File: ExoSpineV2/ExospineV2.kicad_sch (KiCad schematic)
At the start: 30 parts, among them J1 GPIO, J20 S2B-PH-K-S(LF)(SN), J21 S2B-PH-K-S(LF)(SN), J22 S2B-PH-K-S(LF)(SN), J23 S2B-PH-K-S(LF)(SN), J24 Conn_01x02, J25 Conn_01x03, J26 Conn_01x03, J27 Conn_01x04, J28 Conn_01x03, J29 Conn_01x03, Q6 Q_NMOS_DGS, Q7 Q_NMOS_DGS, U6 MCP3008

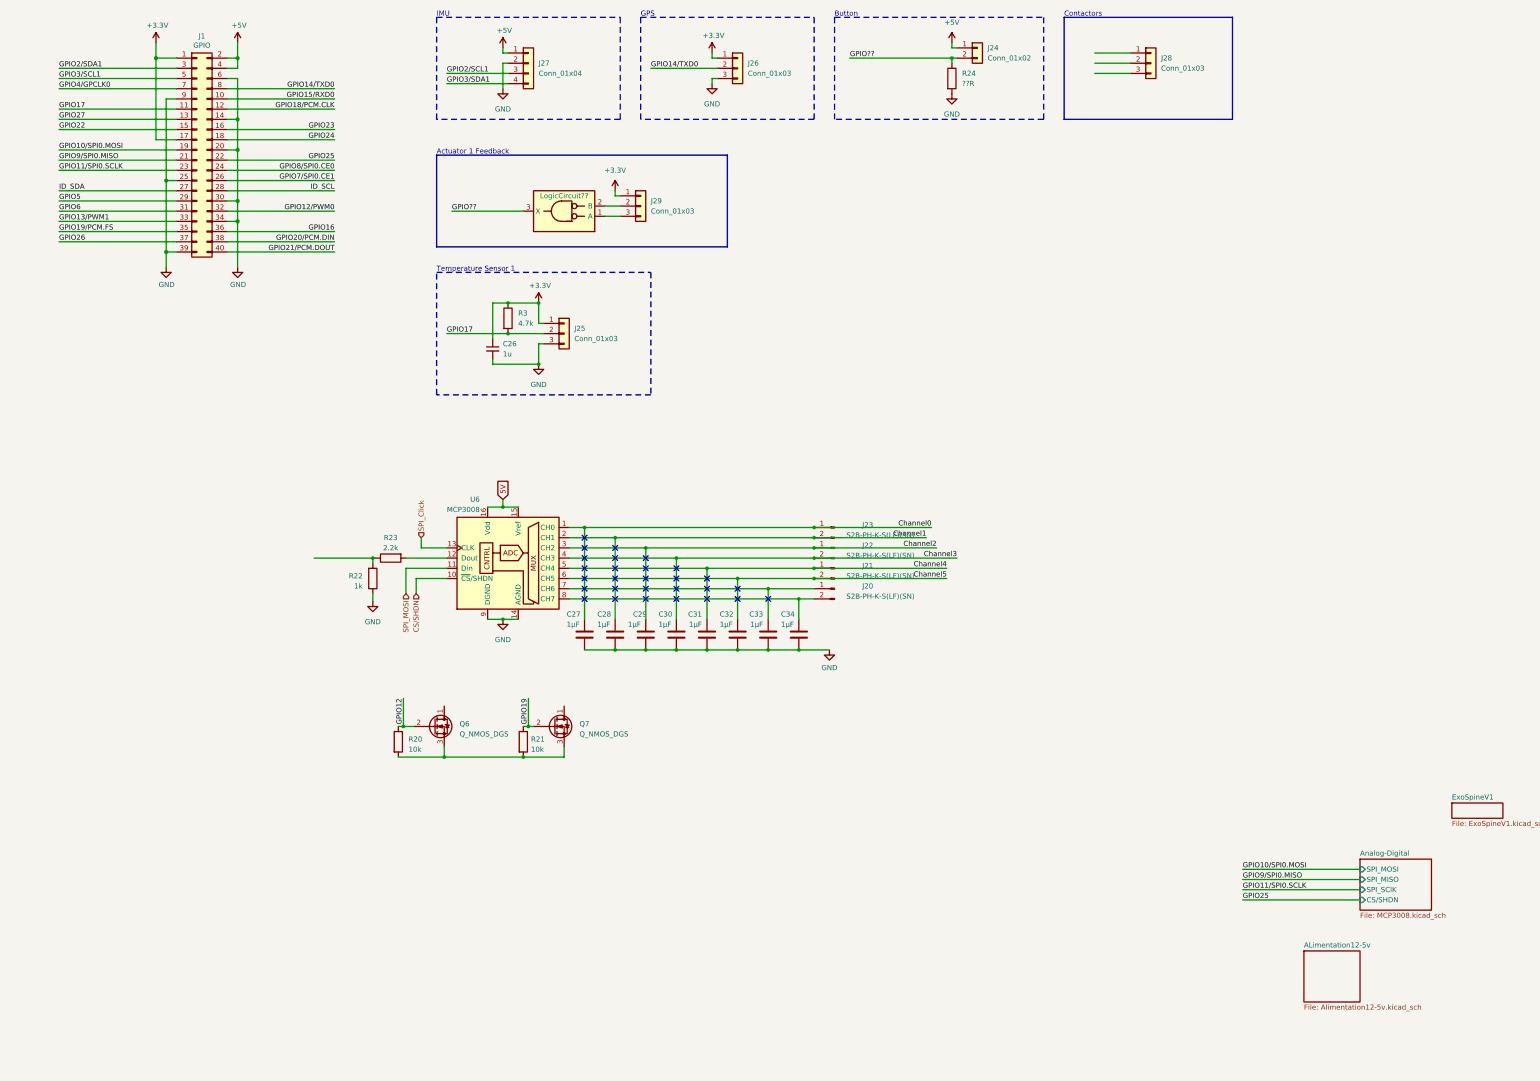
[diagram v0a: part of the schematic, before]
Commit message: MCP3008 circuit
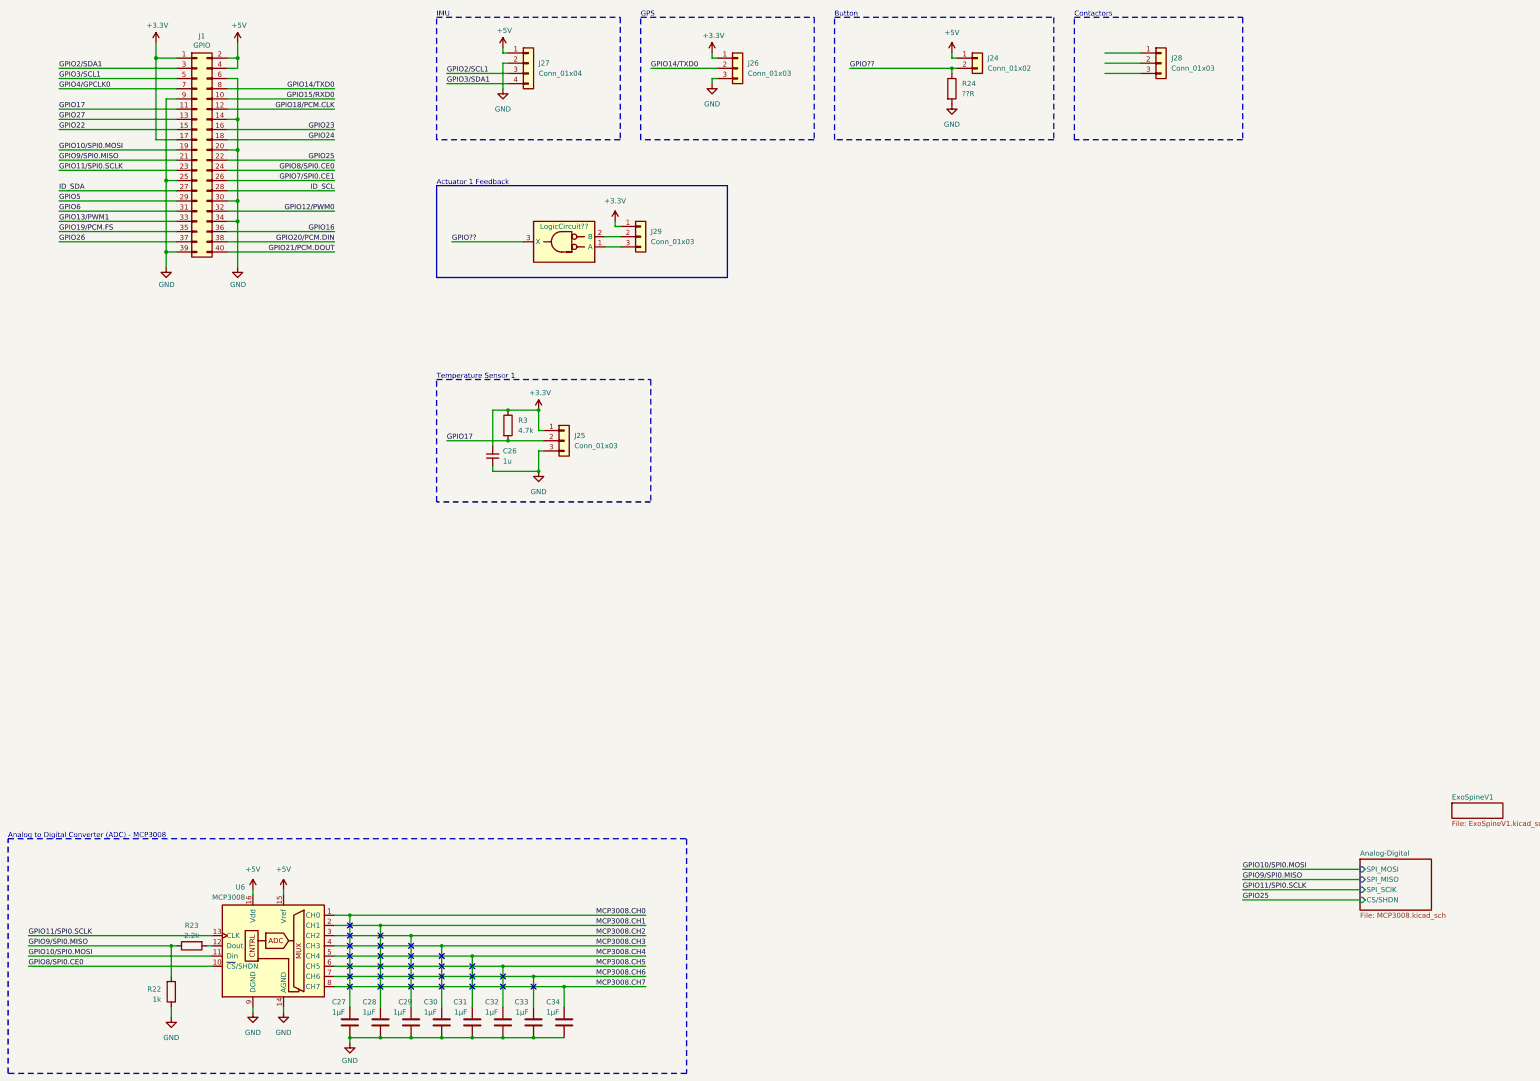
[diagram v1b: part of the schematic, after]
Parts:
- removed J20, J21, J22, J23: S2B-PH-K-S(LF)(SN), Connector_PinHeader_2.00mm:PinHeader_1x02_P2.00mm_Vertical, symbol Connector:Conn_01x02_Pin
- removed Q6, Q7: Q_NMOS_DGS, symbol Device:Q_NMOS_DGS
- removed R20, R21: 10k, symbol Device:R
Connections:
- net 5V is gone; now on net +5V: U6.15 (Vref), U6.16 (Vdd)
- net CS/SHDN is gone; now on net GPIO8/SPI0.CE0: U6.10 (~{CS}/SHDN)
- net SPI_Click is gone; now on net GPIO11/SPI0.SCLK: U6.13 (CLK)
- net SPI_MOSI is gone; now on net GPIO10/SPI0.MOSI: U6.11 (Din)
- net GPIO9/SPI0.MISO: now also R22.2, R23.1
- net MCP3008.CH6: now reaches C33.1, U6.7 (CH6)
- net MCP3008.CH7: now reaches C34.1, U6.8 (CH7)
- net Channel0 renamed MCP3008.CH0
- net Channel1 renamed MCP3008.CH1
- net Channel2 renamed MCP3008.CH2
- net Channel3 renamed MCP3008.CH3
- net Channel4 renamed MCP3008.CH4
- net Channel5 renamed MCP3008.CH5
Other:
- removed sheet ALimentation12-5v
- note added: "Analog to Digital Converter (ADC) - MCP3008"
- moved on the sheet: C26, C27, C28, C29, C30, C31, C32, C33, C34, J24, J25, J28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

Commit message: Actuator Control 1
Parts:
- added J15: Conn_01x02, symbol Connector_Generic:Conn_01x02
- added Q6: Q_NMOS_DGS, symbol Device:Q_NMOS_DGS
- added R10: 10k, symbol Device:R
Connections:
- net GND: now also Q6.3 (S), R10.2
- new net: J15.2 (Pin_2), Q6.1 (D)
- new net +12V: J15.1 (Pin_1)
- new net GPIO12: Q6.2 (G), R10.1
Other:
- removed sheet Analog-Digital
- note added: "Actuator Control 1"
- note added: "Actuator Feedback 1"
- note removed: "Actuator 1 Feedback"
- moved on the sheet: C26, J25, J29, LogicCircuit??, R3

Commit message: Actuator Control 2 and backup
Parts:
- added J16, J17: Conn_01x02, symbol Connector_Generic:Conn_01x02
- added Q7, Q8: Q_NMOS_DGS, symbol Device:Q_NMOS_DGS
- added R11, R12: 10k, symbol Device:R
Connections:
- net GPIO2/SCL1 is gone; now on net GPIO2/SDA1: J27.3 (Pin_3)
- net GPIO3/SDA1 is gone; now on net GPIO3/SCL1: J27.4 (Pin_4)
- net +12V: now also J16.1 (Pin_1), J17.1 (Pin_1)
- net GND: now also Q7.3 (S), Q8.3 (S), R11.2, R12.2
- net GPIO17: no longer J25.2 (Pin_2), R3.2
- net GPIO22: now also Q8.2 (G), R12.1
- net GPIO25: now also J24.2 (Pin_2), R24.1
- net GPIO27: now also Q7.2 (G), R11.1
- net GPIO5: now also J25.2 (Pin_2), R3.2
- net GPIO??: no longer J24.2 (Pin_2), R24.1
- new net: J16.2 (Pin_2), Q7.1 (D)
- new net: J17.2 (Pin_2), Q8.1 (D)
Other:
- note added: "Actuator Control 2"
- note added: "Actuator Control Backup"
- moved on the sheet: C26, J15, J25, J27, Q6, R10, R3

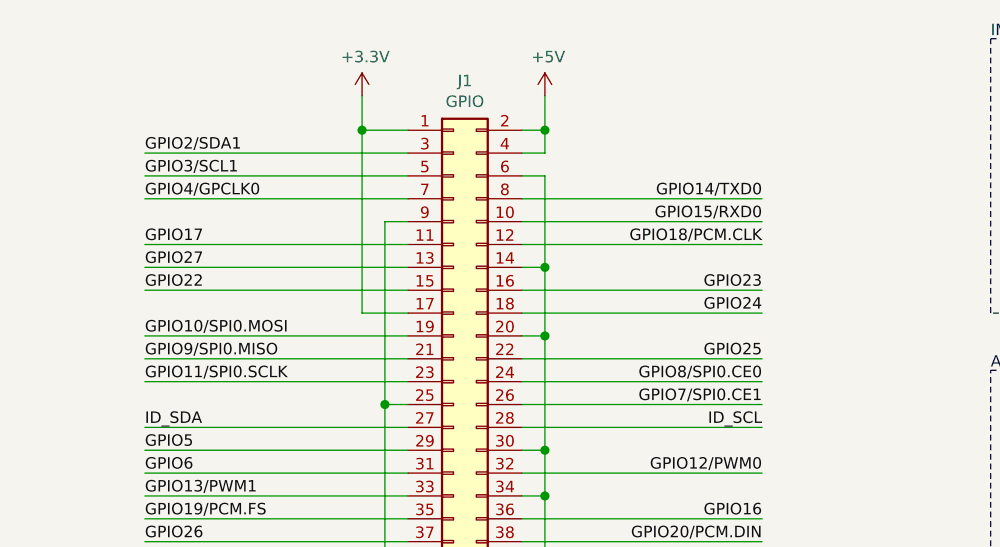
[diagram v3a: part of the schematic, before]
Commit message: Identified RP pins
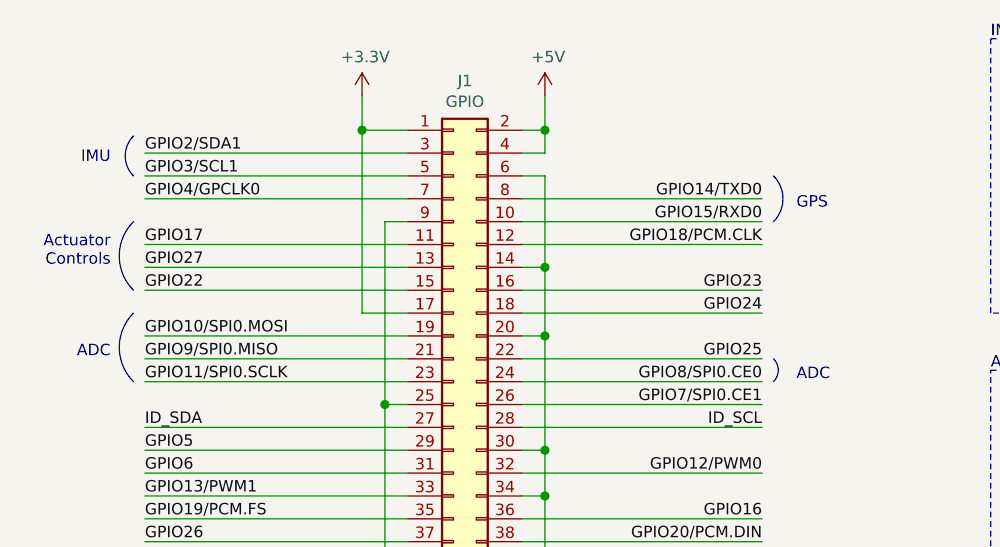
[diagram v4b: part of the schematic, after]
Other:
- note added: "ADC"
- note added: "Actuator Controls"
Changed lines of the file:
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@@
+    (fill (type none))
+  )
+  (arc (start 101.6 33.02) (mid 102.6521 35.56) (end 101.6 38.1)
+    (stroke (width 0) (type default) (color 132 132 132 1))
     (fill (type none))
   )
@@
   (rectangle (start 176.53 17.78) (end 219.71 48.26)
     (stroke (width 0) (type dash))
+    (fill (type none))
+  )
+  (arc (start 30.48 45.72) (mid 28.9019 41.91) (end 30.48 38.1)
+    (stroke (width 0) (type default) (color 132 132 132 1))
     (fill (type none))
   )
@@
     (fill (type none))
   )
+  (arc (start 30.48 55.88) (mid 28.903 52.07) (end 30.48 48.26)
+    (stroke (width 0) (type default) (color 132 132 132 1))
+    (fill (type none))
+  )
   (rectangle (start 19.05 222.25) (end 187.96 280.67)
     (stroke (width 0) (type dash) (color 0 194 0 1))
     (fill (type none))
   )
+  (arc (start 30.48 33.02) (mid 29.564 30.7975) (end 30.48 28.575)
+    (stroke (width 0) (type default) (color 132 132 132 1))
+    (fill (type none))
+  )
+  (arc (start 101.6 53.34) (mid 102.1255 54.61) (end 101.6 55.88)
+    (stroke (width 0) (type default) (color 132 132 132 1))
+    (fill (type none))
+  )
   (text "Actuator Feedback 1 \n" (at 127 156.21 0)
     (effects (font (size 1.27 1.27)) (justify left bottom))
+  )
+  (text "IMU" (at 27.94 31.75 0)
+    (effects (font (size 1.27 1.27) (color 132 132 132 1)) (justify right bottom))
   )
   (text "Actuator Control 1" (at 125.73 54.61 0)
@@
     (effects (font (size 1.27 1.27)) (justify left bottom))
   )
+  (text "Actuator\nControls" (at 27.94 43.18 0)
+    (effects (font (size 1.27 1.27) (color 132 132 132 1)) (justify right bottom))
+  )
+  (text "ADC" (at 27.94 53.34 0)
+    (effects (font (size 1.27 1.27) (color 132 132 132 1)) (justify right bottom))
+  )
   (text "Analog to Digital Converter (ADC) - MCP3008\n" (at 19.05 222.25 0)
     (effects (font (size 1.27 1.27) (color 0 194 0 1)) (justify left bottom))
@@
     (effects (font (size 1.27 1.27)) (justify left bottom))
   )
+  (text "ADC" (at 104.14 55.88 0)
+    (effects (font (size 1.27 1.27) (color 132 132 132 1)) (justify left bottom))
+  )
+  (text "GPS" (at 104.14 36.83 0)
+    (effects (font (size 1.27 1.27) (color 132 132 132 1)) (justify left bottom))
+  )
   (text "GPS" (at 176.53 17.78 0)

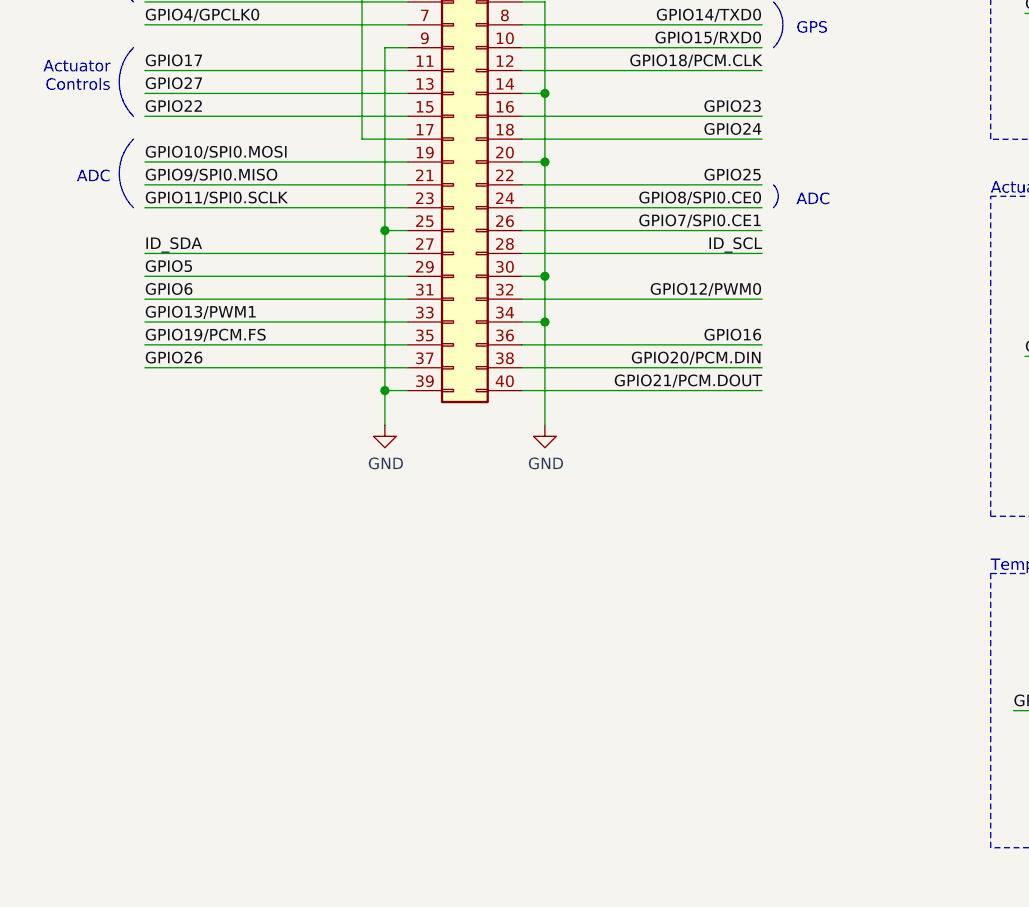
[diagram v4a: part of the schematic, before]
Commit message: Added 12V connector on PCB
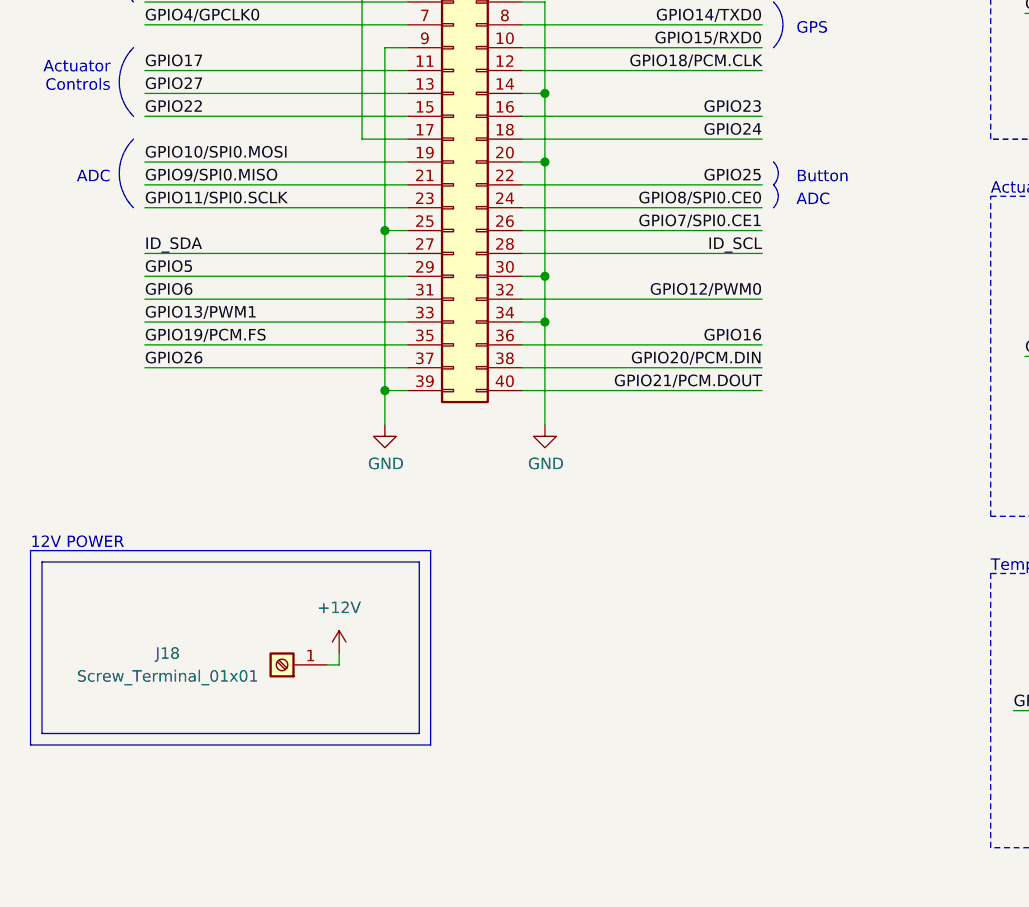
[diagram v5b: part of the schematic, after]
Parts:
- added J18: Screw_Terminal_01x01, symbol Connector:Screw_Terminal_01x01
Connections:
- net +12V: now also J18.1 (Pin_1)
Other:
- note added: "12V POWER"
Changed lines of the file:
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@@
+    (stroke (width 0) (type default))
+  )
+  (wire (pts (xy 53.34 106.68) (xy 52.07 106.68))
     (stroke (width 0) (type default))
   )
@@
   )
   (wire (pts (xy 168.91 168.91) (xy 172.72 168.91))
+    (stroke (width 0) (type default))
+  )
+  (wire (pts (xy 53.34 106.68) (xy 53.34 105.41))
     (stroke (width 0) (type default))
   )
@@
     (fill (type none))
   )
+  (arc (start 101.6 50.8) (mid 102.1261 52.07) (end 101.6 53.34)
+    (stroke (width 0) (type default) (color 132 132 132 1))
+    (fill (type none))
+  )
   (rectangle (start 134.62 222.25) (end 134.62 222.25)
     (stroke (width 0) (type default))
+    (fill (type none))
+  )
+  (rectangle (start 20.32 95.25) (end 62.23 114.3)
+    (stroke (width 0) (type default) (color 194 0 0 1))
     (fill (type none))
   )
@@
     (fill (type none))
   )
+  (rectangle (start 19.05 93.98) (end 63.5 115.57)
+    (stroke (width 0) (type default) (color 194 0 0 1))
+    (fill (type none))
+  )
   (arc (start 101.6 53.34) (mid 102.1255 54.61) (end 101.6 55.88)
     (stroke (width 0) (type default) (color 132 132 132 1))
@@
     (effects (font (size 1.27 1.27)) (justify left bottom))
   )
+  (text "Button" (at 104.14 53.34 0)
+    (effects (font (size 1.27 1.27) (color 132 132 132 1)) (justify left bottom))
+  )
   (text "IMU" (at 27.94 31.75 0)
     (effects (font (size 1.27 1.27) (color 132 132 132 1)) (justify right bottom))
@@
   )
   (text "Actuator Control Backup" (at 252.73 54.61 0)
+    (effects (font (size 1.27 1.27) (color 194 0 0 1)) (justify left bottom))
+  )
+  (text "12V POWER" (at 19.05 93.98 0)
     (effects (font (size 1.27 1.27) (color 194 0 0 1)) (justify left bottom))
   )
@@
     )
   )
+  (symbol (lib_id "power:+12V") (at 53.34 105.41 0) (unit 1)
+    (in_bom yes) (on_board yes) (dnp no) (fields_autoplaced)
+    (property "Reference" "#PWR021" (at 53.34 109.22 0)
+      (effects (font (size 1.27 1.27)) hide)
+    )
+    (property "Value" "+12V" (at 53.34 100.33 0)
+      (effects (font (size 1.27 1.27)))
+    )
+    (property "Footprint" "" (at 53.34 105.41 0)
+      (effects (font (size 1.27 1.27)) hide)
+    )
+    (property "Datasheet" "" (at 53.34 105.41 0)
+      (effects (font (size 1.27 1.27)) hide)
+    )
+    (pin "1")
+    (instances
+      (project "ExospineV2"
+        (path "/e63e39d7-6ac0-4ffd-8aa3-1841a4541b55"
+          (reference "#PWR021") (unit 1)
+        )
+      )
+    )
+  )
   (symbol (lib_name "GND_3") (lib_id "power:GND") (at 194.31 34.29 0) (unit 1)
     (in_bom yes) (on_board yes) (dnp no) (fields_autoplaced)
@@
         )
       )
+    )
+  )
+  (symbol (lib_id "Connector:Screw_Terminal_01x01") (at 46.99 106.68 180) (unit 1)
+    (in_bom yes) (on_board yes) (dnp no)
+    (property "Reference" "J18" (at 34.29 105.41 0)
+      (effects (font (size 1.27 1.27)))
+    )
+    (property "Value" "Screw_Terminal_01x01" (at 34.29 107.95 0)
+      (effects (font (size 1.27 1.27)))
+    )
+    (property "Footprint" "" (at 46.99 106.68 0)
+      (effects (font (size 1.27 1.27)) hide)
+    )
+    (property "Datasheet" "~" (at 46.99 106.68 0)
+      (effects (font (size 1.27 1.27)) hide)
+    )
+    (pin "1")
+    (instances
+      (project "ExospineV2"
+        (path "/e63e39d7-6ac0-4ffd-8aa3-1841a4541b55"
+          (reference "J18") (unit 1)
+        )
+      )

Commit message: Added Pressure Sensors 1 and 2
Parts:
- added J19, J20: Conn_01x03, symbol Connector_Generic:Conn_01x03
- added R13, R14: 10k, symbol Device:R
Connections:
- net +12V: now also J19.1 (Pin_1), J20.1 (Pin_1)
- net GND: now also J19.3 (Pin_3), J20.3 (Pin_3), R13.2, R14.2
- net MCP3008.CH0: now also J19.2 (Pin_2), R14.1
- net MCP3008.CH1: now also J20.2 (Pin_2), R13.1
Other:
- note added: "Pressure Sensor 1"
- note added: "Pressure Sensor 2"
- moved on the sheet: C26, C27, C28, C29, C30, C31, C32, C33, C34, J15, J16, J17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
